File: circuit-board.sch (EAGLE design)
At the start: 45 parts, among them U1 ADUM1201BRZ, U4 TL071CD, U5 MAX3232, U6 LD11175.0S33TR, U7 ATMEGA328P_TQFP, Y1 16MHz

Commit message: This worked great with my USB soundcard but not at all with the radio, giving up on this approach -- a BC547 does the trick and eliminates a bunch of isolation and some battery usage
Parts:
- removed C18: 0.1uF, SparkFun-Capacitors:0.1UF-0603-25V-5%
- added C3: 27pF, SparkFun-Capacitors:27PF-0603-50V-5%
- added U2: OPA2134UA, Texas Instruments_By_element14_Batch_1:OPA2134UA
- added UC-DBG, UC-SER, UC-SS: (no value), SparkFun-Connectors:CONN_02
- C17: value 0.1uF -> 27pF; device SparkFun-Capacitors:0.1UF-0603-25V-5% -> SparkFun-Capacitors:27PF-0603-50V-5%
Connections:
- removed net N$14: U5.R1OUT, U7.PD0(RXD)
- removed net N$19: U5.T1IN, U7.PD1(TXD)
- new net UC-DBG-RX: U7.PD7(AIN1), UC-DBG.1
- new net UC-DBG-TX: U7.PD6(AIN0), UC-DBG.2
- new net UC-RX: U5.R1OUT, U7.PD0(RXD), UC-SER.1
- new net UC-TX: U5.T1IN, U7.PD1(TXD), UC-SER.2
- net GNDA: now also C17.1, C3.1; no longer C17.2, C18.2
- net N$23: now also C3.2; no longer C17.1
- net N$24: now also C17.2; no longer C18.1
- net UC-SS-RX: now also UC-SS.1
- net UC-SS-TX: now also UC-SS.2
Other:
- moved on the sheet: C17, C19, C20, JP1, U1

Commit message: Circuit schematic finalized, laying out PCB now
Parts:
- removed 12V: JST-XH-02-PIN-LONG-PAD, Rembrandt Electronics - JST XH Connectors v1-0:JST-XH-02-PIN-LONG-PAD
- removed C16, C19, C20: 0.1uF, SparkFun-Capacitors:0.1UF-0603-25V-5%
- removed C17: 27pF, SparkFun-Capacitors:27PF-0603-50V-5%
- removed JP1: (no value), arduino_jw:ARDUINO_CONN-ICSP
- removed OK1: 4N25SM, optocoupler:4N25SM
- removed R10: 1k, SparkFun-Resistors:1KOHM-0603-1/10W-1%
- removed R11: 10k, SparkFun-Resistors:10KOHM-0603-1/10W-1%
- removed R6: 390, SparkFun-Resistors:390OHM-0603-1/10W-1%
- removed R7: 2.2k, SparkFun-Resistors:2.2KOHM-0603-1/10W-1%
- removed R8: 22k, SparkFun-Resistors:22KOHM-0603-1/10W-1%
- removed R9: 10k, SparkFun-Retired:TRIMPOTTRIMPOT_PTH_S3_LOCK
- removed TR2: 42TL013, trafo-xicon:42TL013
- removed TR3: 42TL016, trafo-xicon:42TL016
- removed U-283: JST-XH-06-PIN-LONG-PAD, Rembrandt Electronics - JST XH Connectors v1-0:JST-XH-06-PIN-LONG-PAD
- removed U4: TL071CD, Texas Instruments_By_element14_Batch_1:TL071CD
- removed U5: MAX3232, SparkFun-IC-Comms:MAX2323SOIC16
- removed U6: LD11175.0S33TR, Ai_Power:LD11175.0S33TR
- removed U7: ATMEGA328P_TQFP, SparkFun-IC-Microcontroller:ATMEGA328P_TQFP
- added 12V-IN, 5V-USB: JST-XH-02-PIN-LONG-PAD, Rembrandt Electronics - JST XH Connectors v1-0:JST-XH-02-PIN-LONG-PAD
- added 5V-OUT: JST-XH-03-PIN-LONG-PAD, Rembrandt Electronics - JST XH Connectors v1-0:JST-XH-03-PIN-LONG-PAD
- added EXP-GND, EXT-GND: (no value), SparkFun-Connectors:CONN_02
- added HANDSET: JST-XH-06-PIN-LONG-PAD, Rembrandt Electronics - JST XH Connectors v1-0:JST-XH-06-PIN-LONG-PAD
- added ICSP: (no value), arduino_jw:ARDUINO_CONN-ICSP
- added Q1: BC547B, transistor-npn:BC547B
- added U3: ADUM1201BRZ, Analog Devices_By_element14_Batch_1:ADUM1201BRZ
- C1, C9: value 0.1uF -> 10uF
- C12, C13: value 0.1uF -> 27pF; device SparkFun-Capacitors:0.1UF-0603-25V-5% -> SparkFun-Capacitors:27PF-0603-50V-5%
- C3: value 27pF -> 0.1uF; device SparkFun-Capacitors:27PF-0603-50V-5% -> SparkFun-Capacitors:0.1UF-0603-25V-5%
- C4: value 100uF -> 0.1uF; device adafruit:CPOL-USE2.5-5 -> SparkFun-Capacitors:0.1UF-0603-25V-5%
- C6, C7, C8: value 10uF -> 0.1uF; device adafruit:CPOL-USE2.5-5 -> SparkFun-Capacitors:0.1UF-0603-25V-5%
- R1: value 1k -> 22k; device SparkFun-Resistors:1KOHM-0603-1/10W-1% -> SparkFun-Resistors:22KOHM-0603-1/10W-1%
- R2: value 220k -> (none); device SparkFun-Resistors:220KOHM-0603-1/10W-1% -> resistor:R-TRIMMT93YA
- R3: value 1M -> 2.0k; device SparkFun-Resistors:1MOHM-0603-1/4W-5% -> SparkFun-Resistors:2.0KOHM-0603-1/10W-5%
- R4: value 1M -> 2.2k; device SparkFun-Resistors:1MOHM-0603-1/4W-5% -> SparkFun-Resistors:2.2KOHM-0603-1/10W-1%
- R5: value 10 -> 10k; device SparkFun-Resistors:10OHM-0603-1/10W-1% -> SparkFun-Resistors:10KOHM-0603-1/10W-1%
- U1: value ADUM1201BRZ -> MAX3232; device Analog Devices_By_element14_Batch_1:ADUM1201BRZ -> SparkFun-IC-Comms:MAX2323SOIC16
- U2: value OPA2134UA -> ATMEGA328P_TQFP; device Texas Instruments_By_element14_Batch_1:OPA2134UA -> SparkFun-IC-Microcontroller:ATMEGA328P_TQFP
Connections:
- removed net 5V: C12.1, C15.2, C20.1, C8.+, C9.+, JP1.2, R11.2, R3.1, R5.1, R6.2, U1.VDD1, U5.VCC, U6.OUT, U7.AVCC, U7.VCC@4, U7.VCC@6
- removed net GPS-SIG-GND: GPS-2.S
- removed net N$1: C2.+, R3.2, R4.2, U4.IN+
- removed net N$10: R9.WIPER, TR3.1
- removed net N$11: C6.-, TR3.6
- removed net N$13: C5.-, R9.CCW
- removed net N$2: R1.2, R2.1, U4.IN-
- removed net N$5: C1.+, R1.1
- removed net N$6: C5.+, R2.2, U4.OUT
- removed net N$7: OK1.A, R6.1
- removed net N$8: OK1.EMI, R7.2
- removed net N$9: C4.+, R5.2, U4.VCC+
- new net +5V: 5V-OUT-2.S, 5V-OUT-3.S, 5V-USB-2.S, C1.+, C11.2, C15.1, C2.+, C6.1, ICSP.2, R5.2, U1.VCC, U2.AVCC, U2.VCC@4, U2.VCC@6, U3.VDD1
- new net GND2: 12V-IN-1.S, GPS-1.S
- new net N$3: C9.+, Q1.C, R2.S, R3.1
- new net N$4: C5.+, Q1.B, R2.E
- net 12V: now also 12V-IN-2.S; no longer 12V-2.S, C7.+, U6.IN
- net 3.3V: now also C14.1, R1.2, R3.2, U3.VDD2; no longer C19.1, R8.2, U1.VDD2
- net GND: now also C14.2, EXP-GND.1, EXT-GND.1, HANDSET-1.S, Q1.E, U3.GND2; no longer C19.2, R7.1, TR2.4, TR3.4, U1.GND2
- net GNDA: now also 5V-OUT-1.S, 5V-USB-1.S, C1.-, C10.2, C11.1, C12.1, C13.1, C15.2, C6.2, C7.2, C8.2, GPS-2.S, ICSP.6, U1.GND, U2.AGND, U2.GND@3, U2.GND@5, U3.GND1; no longer 12V-1.S, C12.2, C13.2, C14.2, C15.1, C16.2, C17.1, C20.2, C3.1, C4.-, C7.-, C8.-, C9.-, GPS-1.S, JP1.6, R10.1, R4.1, R9.CW, TR2.3, TR3.3, U-283-1.S, U1.GND1, U4.VCC-, U5.GND, U7.AGND, U7.GND@3, U7.GND@5
- net GPS-RX: now also U1.T1OUT; no longer U5.T1OUT
- net GPS-TX: now also U1.R1IN; no longer U5.R1IN
- net HANDSET-EXP: now also EXP-GND.2, HANDSET-5.S; no longer U-283-5.S
- net HANDSET-EXT: now also EXT-GND.2, HANDSET-6.S; no longer U-283-6.S
- net HANDSET-MIC: now also C5.-, HANDSET-4.S; no longer C1.-, R10.2, U-283-4.S
- net HANDSET-PTT: now also HANDSET-3.S, R4.1; no longer OK1.C, U-283-3.S
- net HANDSET-SPK: now also HANDSET-2.S; no longer TR2.1, U-283-2.S
- net N$12: now also R1.1; no longer R8.1
- net N$15: now also C3.2, U1.C1-; no longer C11.2, U5.C1-
- net N$16: now also C3.1, U1.C1+; no longer C11.1, U5.C1+
- net N$17: now also C4.2, U1.C2-; no longer C10.2, U5.C2-
- net N$18: now also C4.1, U1.C2+; no longer C10.1, U5.C2+
- net N$20: now also C7.1, U1.V+; no longer C13.1, U5.V+
- net N$21: now also C8.1, U1.V-; no longer C14.1, U5.V-
- net N$22: now also C10.1, U2.AREF; no longer C16.1, U7.AREF
- net N$23: now also C12.2, U2.PB6(XTAL1/TOSC1); no longer C3.2, U7.PB6(XTAL1/TOSC1)
- net N$24: now also C13.2, U2.PB7(XTAL2/TOSC2); no longer C17.2, U7.PB7(XTAL2/TOSC2)
- net RADIO-MIC/PTT: now also C9.-, R4.2; no longer C6.+, OK1.COL
- net RADIO-RX: now also U3.VOB; no longer U1.VOB
- net RADIO-SPK-OUT: no longer TR2.6
- net RADIO-TX: now also U3.VIA; no longer U1.VIA
- net UC-DBG-RX: now also U2.PD7(AIN1); no longer U7.PD7(AIN1)
- net UC-DBG-TX: now also U2.PD6(AIN0); no longer U7.PD6(AIN0)
- net UC-MISO: now also ICSP.1, U2.PB4(MISO); no longer JP1.1, U7.PB4(MISO)
- net UC-MOSI: now also ICSP.4, U2.PB3(MOSI/OC2); no longer JP1.4, U7.PB3(MOSI/OC2)
- net UC-RESET: now also ICSP.5, R5.1, U2.PC6(/RESET); no longer JP1.5, R11.1, U7.PC6(/RESET)
- net UC-RX: now also U1.R1OUT, U2.PD0(RXD); no longer U5.R1OUT, U7.PD0(RXD)
- net UC-SCK: now also ICSP.3, U2.PB5(SCK); no longer JP1.3, U7.PB5(SCK)
- net UC-SS-RX: now also U2.PB1(OC1A), U3.VOA; no longer U1.VOA, U7.PB1(OC1A)
- net UC-SS-TX: now also U2.PB0(ICP), U3.VIB; no longer U1.VIB, U7.PB0(ICP)
- net UC-TX: now also U1.T1IN, U2.PD1(TXD); no longer U5.T1IN, U7.PD1(TXD)
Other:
- moved on the sheet: C1, C10, C11, C12, C13, C14, C15, C2, C3, C5, C9, GPS-1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

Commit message: Added 0 Ohm resistor to avoid renaming nets, finished initial PCB layout
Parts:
- added R6: 0, SparkFun-Resistors:0OHM-0603-1/10W-5%
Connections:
- net HANDSET-SPK: now also R6.1
- net RADIO-SPK-OUT: now also R6.2
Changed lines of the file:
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@@
 <setting verticaltext="up"/>
 </settings>
-<grid distance="0.1" unitdist="inch" unit="inch" style="lines" multiple="1" display="yes" altdistance="0.01" altunitdist="inch" altunit="inch"/>
+<grid distance="0.1" unitdist="inch" unit="inch" style="lines" multiple="1" display="no" altdistance="0.01" altunitdist="inch" altunit="inch"/>
 <layers>
 <layer number="1" name="Top" color="4" fill="1" visible="no" active="no"/>
@@
 <part name="P+2" library="SparkFun" deviceset="3.3V" device=""/>
 <part name="GND1" library="supply1" deviceset="GNDA" device=""/>
-<part name="C1" library="adafruit" deviceset="CPOL-US" device="E2.5-5" value="10uF"/>
-<part name="C2" library="adafruit" deviceset="CPOL-US" device="E2.5-5" value="0.1uF"/>
+<part name="C1" library="adafruit" library_urn="urn:adsk.eagle:library:420" deviceset="CPOL-US" device="E2.5-5" value="10uF"/>
+<part name="C2" library="adafruit" library_urn="urn:adsk.eagle:library:420" deviceset="CPOL-US" device="E2.5-5" value="0.1uF"/>
 <part name="SPK-SW" library="SparkFun-Connectors" deviceset="CONN_02" device=""/>
 <part name="RADIO" library="Rembrandt Electronics - JST XH Connectors v1-0" deviceset="JST-XH-07-PIN" device="-LONG-PAD"/>
@@
 <part name="EXT-GND" library="SparkFun-Connectors" deviceset="CONN_02" device=""/>
 <part name="Q1" library="transistor-npn" library_urn="urn:adsk.eagle:library:398" deviceset="BC547*" device="" package3d_urn="urn:adsk.eagle:package:28974/2" technology="B"/>
-<part name="C9" library="adafruit" deviceset="CPOL-US" device="E2.5-5" value="10uF"/>
-<part name="C5" library="adafruit" deviceset="CPOL-US" device="E2.5-5" value="10uF"/>
+<part name="C9" library="adafruit" library_urn="urn:adsk.eagle:library:420" deviceset="CPOL-US" device="E2.5-5" value="10uF"/>
+<part name="C5" library="adafruit" library_urn="urn:adsk.eagle:library:420" deviceset="CPOL-US" device="E2.5-5" value="10uF"/>
 <part name="P+3" library="SparkFun" deviceset="3.3V" device=""/>
 <part name="R3" library="SparkFun-Resistors" deviceset="2.0KOHM" device="-0603-1/10W-5%" value="2.0k"/>
@@
 <part name="GND11" library="supply1" deviceset="GND" device=""/>
 <part name="V1" library="supply4" deviceset="+5V" device=""/>
+<part name="R6" library="SparkFun-Resistors" deviceset="0OHM" device="-0603-1/10W-5%" value="0"/>
 </parts>
 <sheets>
@@
 <instance part="GND11" gate="1" x="-177.8" y="127" rot="R90"/>
 <instance part="V1" gate="1" x="-287.02" y="129.54"/>
+<instance part="R6" gate="G$1" x="45.72" y="220.98"/>
 </instances>
 <busses>
@@
 <label x="-218.44" y="241.3" size="1.778" layer="95"/>
 </segment>
+<segment>
+<pinref part="R6" gate="G$1" pin="1"/>
+<wire x1="40.64" y1="220.98" x2="20.32" y2="220.98" width="0.1524" layer="91"/>
+<label x="20.32" y="220.98" size="1.778" layer="95"/>
+</segment>
 </net>
 <net name="HANDSET-PTT" class="0">
@@
 <label x="-220.98" y="210.82" size="1.778" layer="95"/>
 </segment>
-</net>
+<segment>
+<pinref part="R6" gate="G$1" pin="2"/>
+<wire x1="50.8" y1="220.98" x2="73.66" y2="220.98" width="0.1524" layer="91"/>
+<label x="53.34" y="220.98" size="1.778" layer="95"/>
+</segment>
+</net>

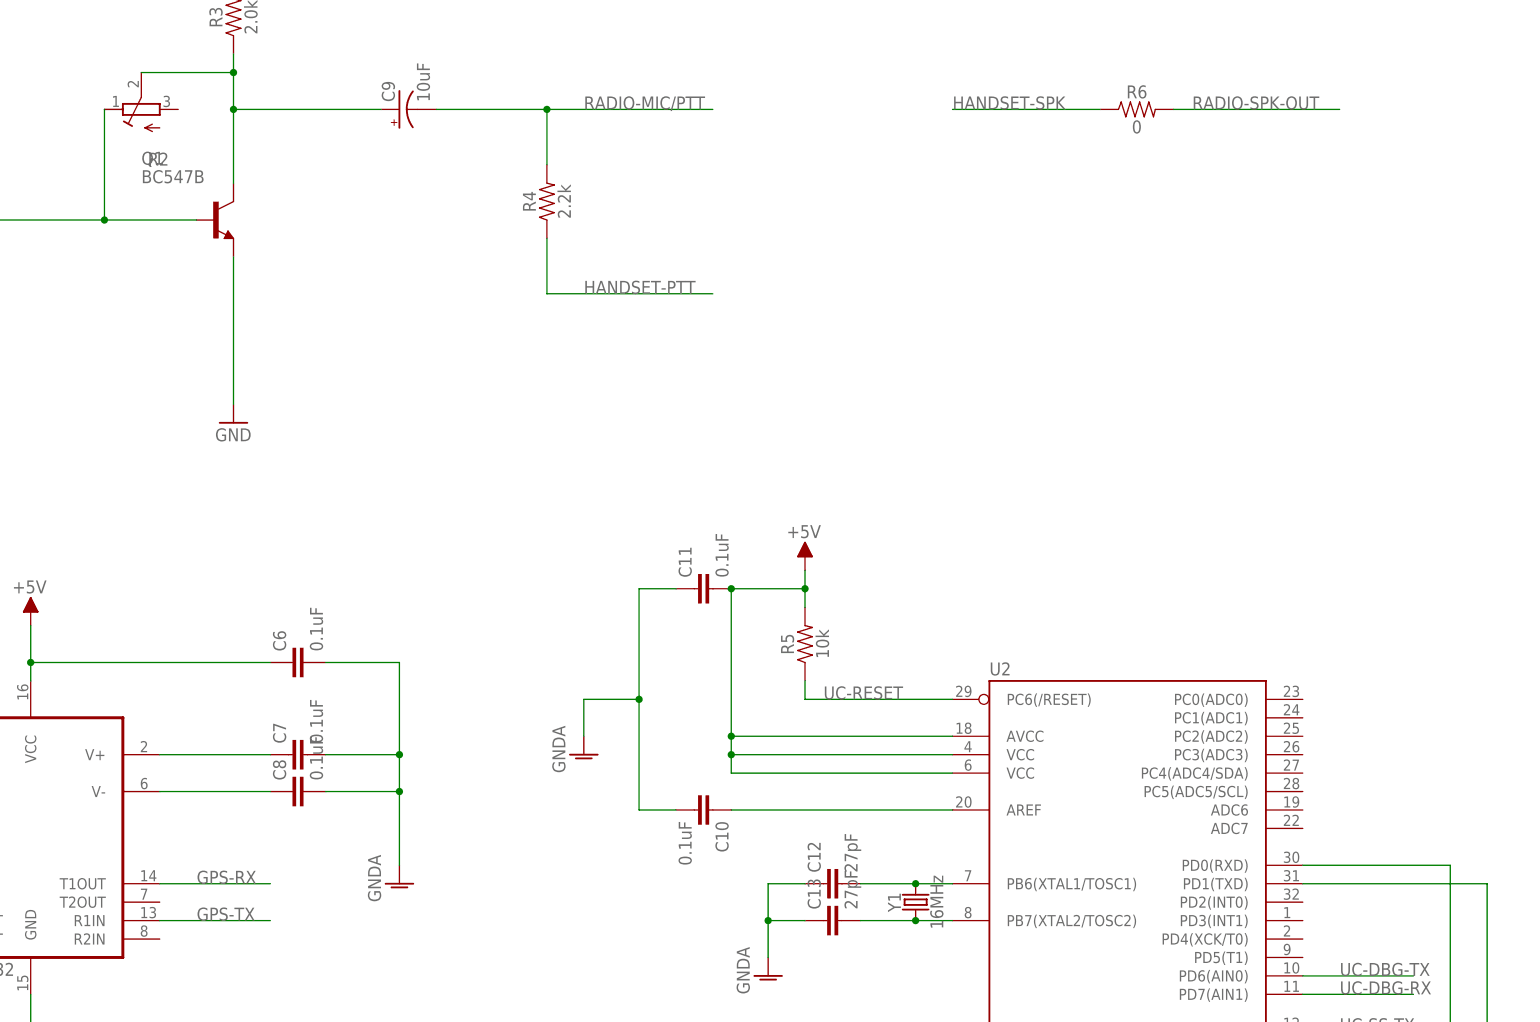
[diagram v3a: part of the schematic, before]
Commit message: Done for tonight, PCB laid out, need to verify ERC/DRC tomorrow
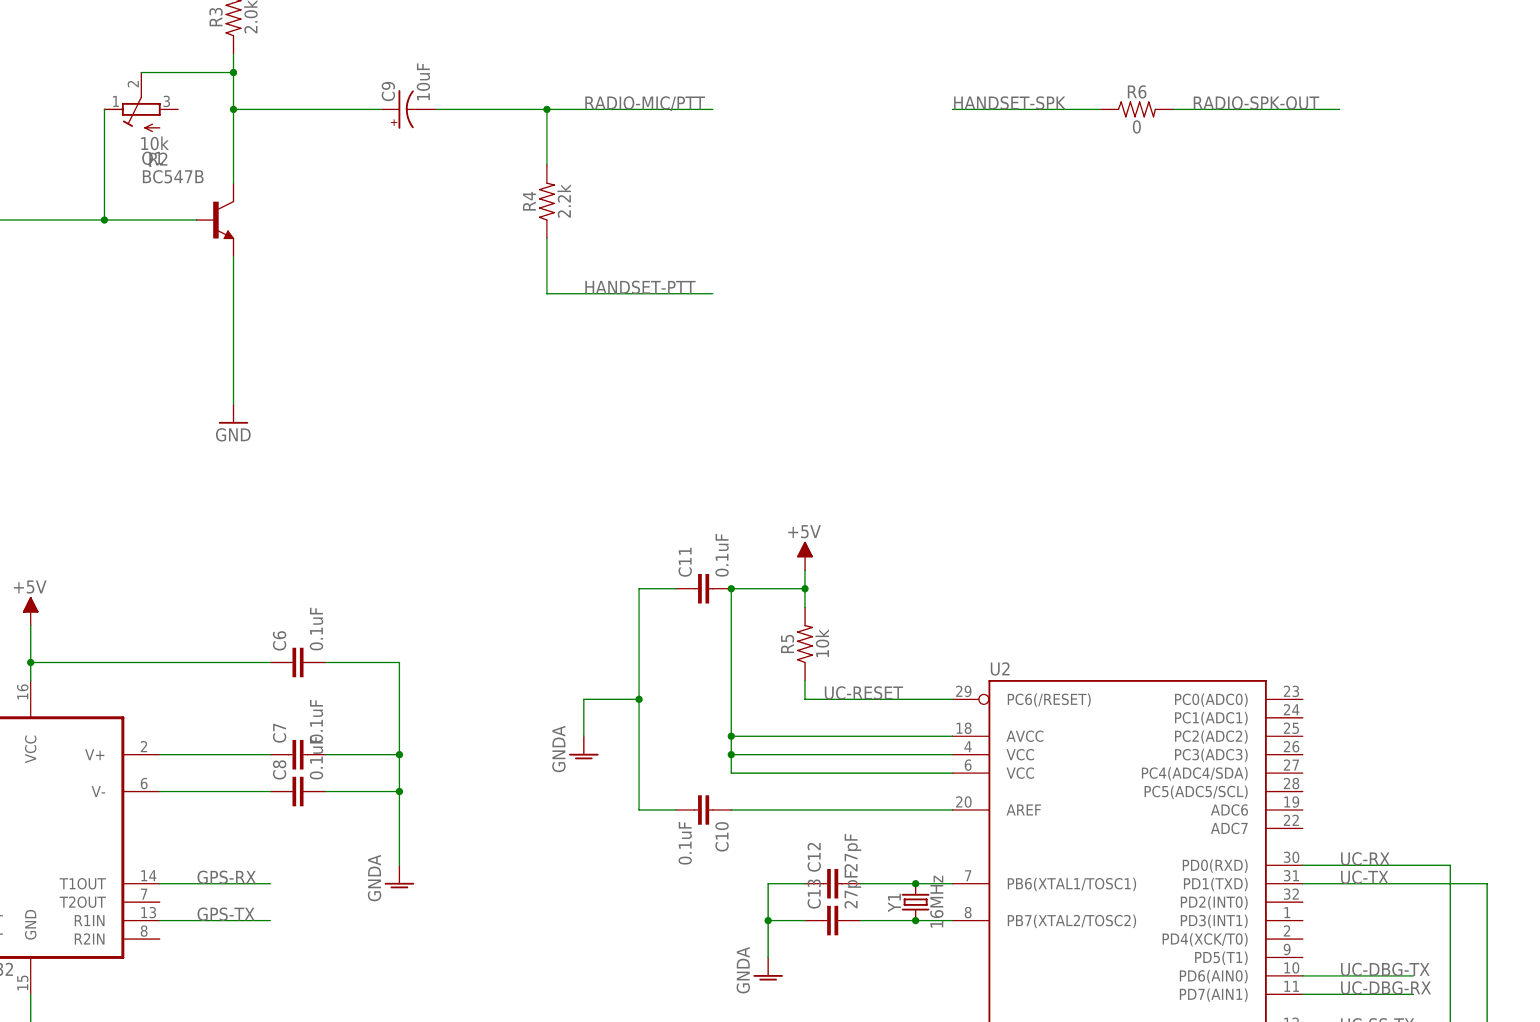
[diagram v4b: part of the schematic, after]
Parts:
- R2: value (none) -> 10k
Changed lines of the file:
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@@
 <part name="P+3" library="SparkFun" deviceset="3.3V" device=""/>
 <part name="R3" library="SparkFun-Resistors" deviceset="2.0KOHM" device="-0603-1/10W-5%" value="2.0k"/>
-<part name="R2" library="resistor" library_urn="urn:adsk.eagle:library:348" deviceset="R-TRIMM" device="T93YA" package3d_urn="urn:adsk.eagle:package:26051/1"/>
+<part name="R2" library="resistor" library_urn="urn:adsk.eagle:library:348" deviceset="R-TRIMM" device="T93YA" package3d_urn="urn:adsk.eagle:package:26051/1" value="10k"/>
 <part name="R4" library="SparkFun-Resistors" deviceset="2.2KOHM" device="-0603-1/10W-1%" value="2.2k"/>
 <part name="GND13" library="supply1" deviceset="GND" device=""/>
@@
 <pinref part="U2" gate="U$1" pin="PD0(RXD)"/>
 <wire x1="88.9" y1="116.84" x2="68.58" y2="116.84" width="0.1524" layer="91"/>
+<label x="73.66" y="116.84" size="1.778" layer="95"/>
 </segment>
 <segment>
@@
 <pinref part="U2" gate="U$1" pin="PD1(TXD)"/>
 <wire x1="93.98" y1="114.3" x2="68.58" y2="114.3" width="0.1524" layer="91"/>
+<label x="73.66" y="114.3" size="1.778" layer="95"/>
 </segment>
 <segment>
@@
 </sheet>
 </sheets>
+<errors>
+</errors>
 </schematic>
 </drawing>

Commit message: Added voltage regulator, dropped some JSTs, relaid out board, rerouted
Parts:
- removed 5V-OUT: JST-XH-03-PIN-LONG-PAD, Rembrandt Electronics - JST XH Connectors v1-0:JST-XH-03-PIN-LONG-PAD
- removed 5V-USB: JST-XH-02-PIN-LONG-PAD, Rembrandt Electronics - JST XH Connectors v1-0:JST-XH-02-PIN-LONG-PAD
- removed C1: 10uF, adafruit:CPOL-USE2.5-5
- removed C2: 0.1uF, adafruit:CPOL-USE2.5-5
- added C16, C20: 10uF, adafruit:CPOL-USE2.5-5
- added C17, C19: 0.1uF, SparkFun-Capacitors:0.1UF-0603-25V-5%
- added C18: 10nF, SparkFun-Capacitors:10NF-0603-50V-10%
- added FB1: 30Ω/1.8A, SparkFun-Coils:FERRITE_BEAD-0603
- added U4: UA78M05CDCY, Texas Instruments_By_element14_Batch_1:UA78M05CDCY
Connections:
- removed net GND2: 12V-IN-1.S, GPS-1.S
- new net N$1: C16.+, C17.1, FB1.2, U4.INPUT
- net +5V: now also C19.1, C20.+, U4.OUTPUT; no longer 5V-OUT-2.S, 5V-OUT-3.S, 5V-USB-2.S, C1.+, C2.+
- net 12V: now also C18.1, FB1.1
- net GNDA: now also 12V-IN-1.S, C16.-, C17.2, C18.2, C19.2, C20.-, GPS-1.S, U4.COMMON, U4.COMMON_2; no longer 5V-OUT-1.S, 5V-USB-1.S, C1.-, C2.-
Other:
- moved on the sheet: 12V-IN-1, 12V-IN-2, EXP-GND, EXT-GND, ICSP, R1, R6, SPK-SW, UC-DBG, UC-SER, UC-SS
